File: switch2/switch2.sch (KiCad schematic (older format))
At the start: 19 parts, among them J1 Screw_Terminal_01x02, J2 Screw_Terminal_01x02, J3 Conn_01x16, K1 FINDER-40.31, Q1 Q_NPN_BCE, Q2 Q_NPN_BCE, U1 KAQV214, U2 KAQV214

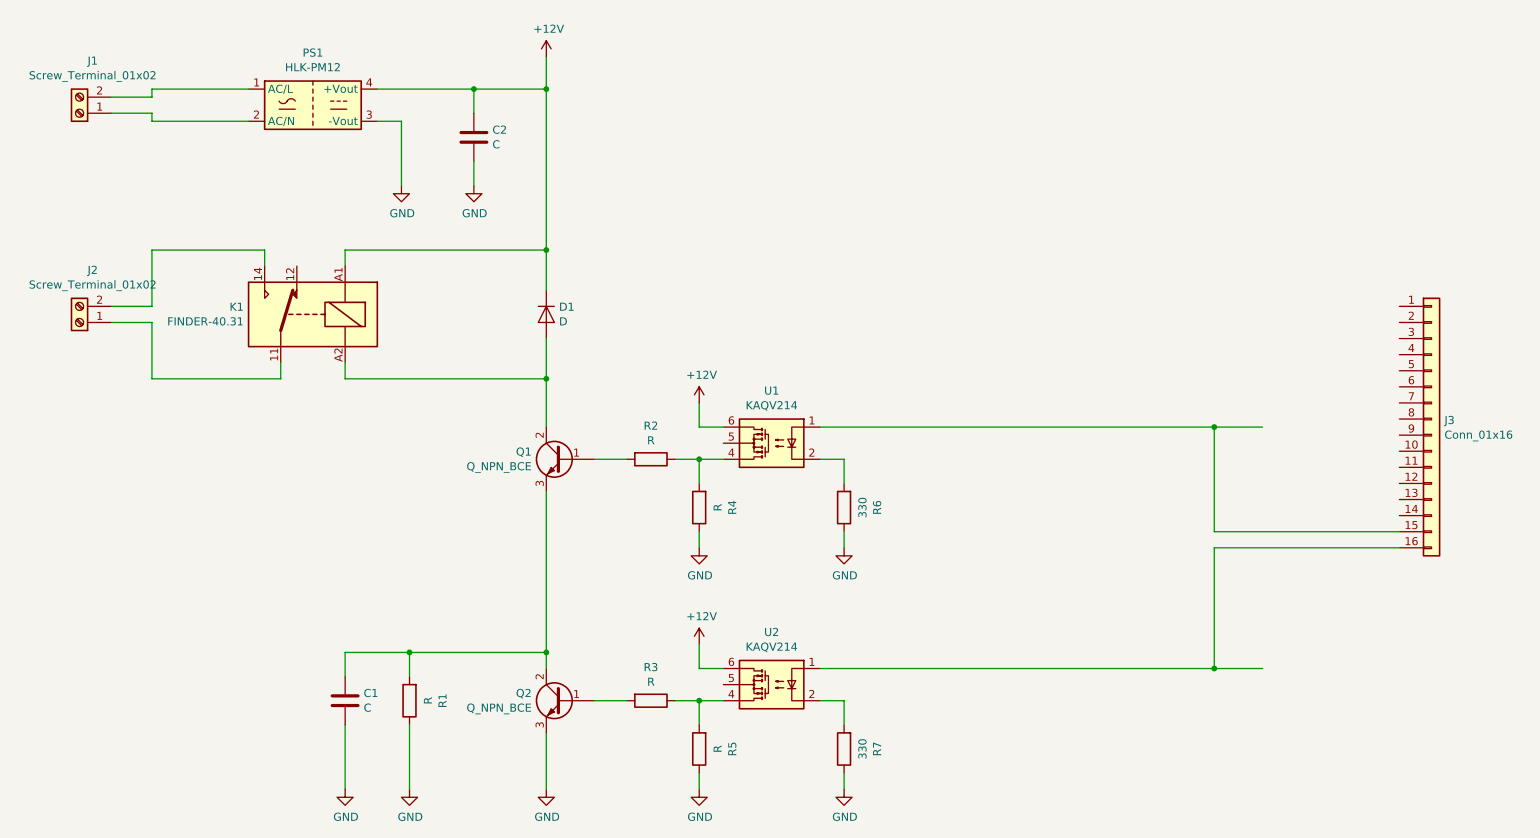
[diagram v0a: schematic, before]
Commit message: Removed transistors that might not be needed.
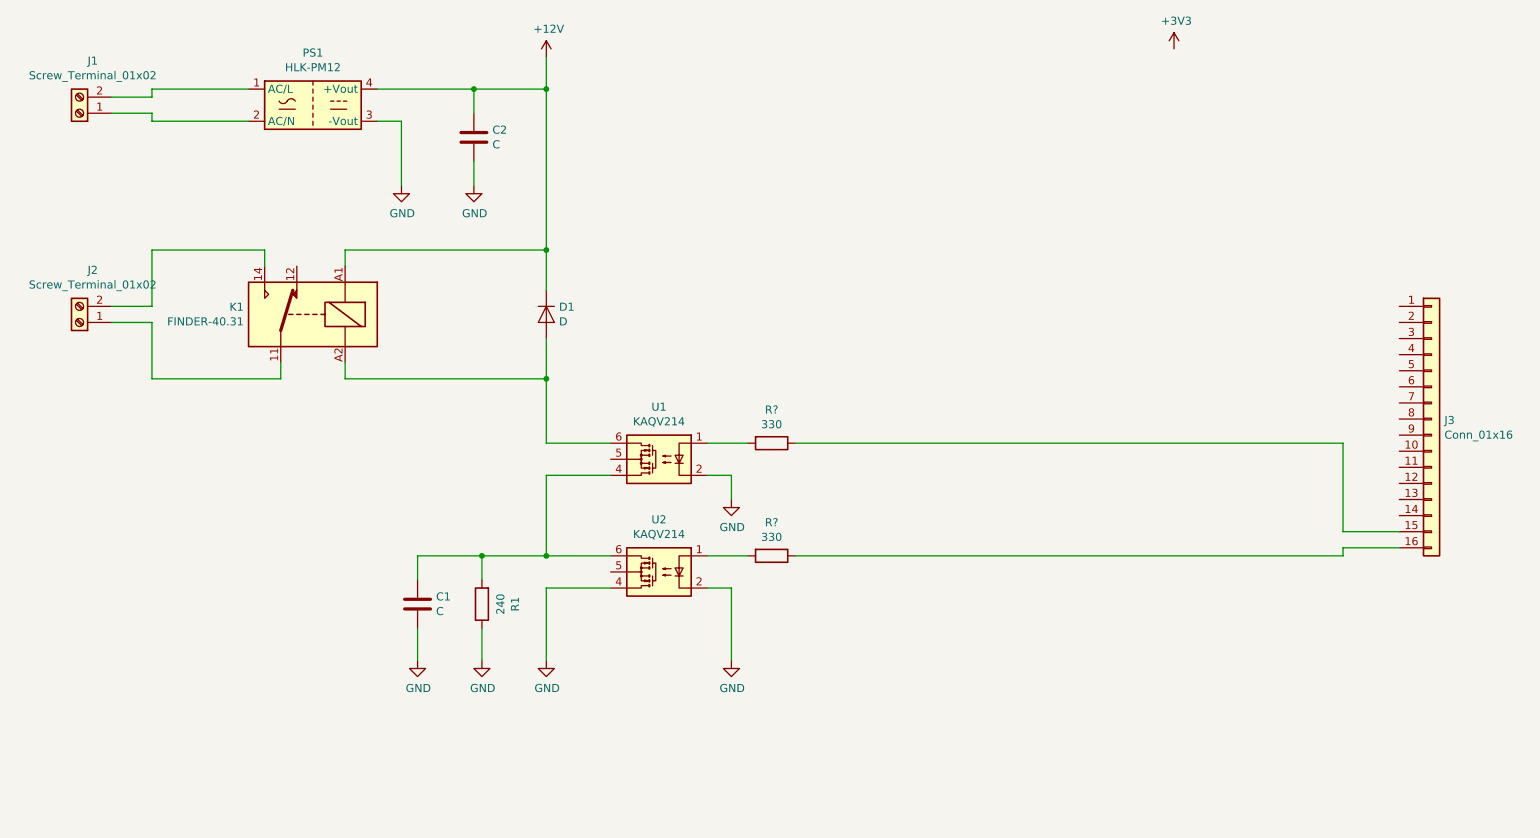
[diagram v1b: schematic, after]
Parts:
- removed Q1, Q2: Q_NPN_BCE, symbol Device:Q_NPN_BCE
- removed R2, R3, R4, R5: R, symbol Device:R
- removed R6, R7: 330, symbol Device:R
- added R? (x2): 330, symbol Device:R
- R1: value R -> 240
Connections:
- net labels added: +3V3
- wire segments 66 -> 53
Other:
- moved on the sheet: C1, R1, U1, U2
